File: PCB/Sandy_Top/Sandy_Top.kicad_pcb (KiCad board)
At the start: 2 copper layers, 285 x 37 mm, 63 parts, among them J1 Conn_02x02_Top_Bottom, J2 Conn_02x02_Top_Bottom, J3 Conn_02x02_Top_Bottom

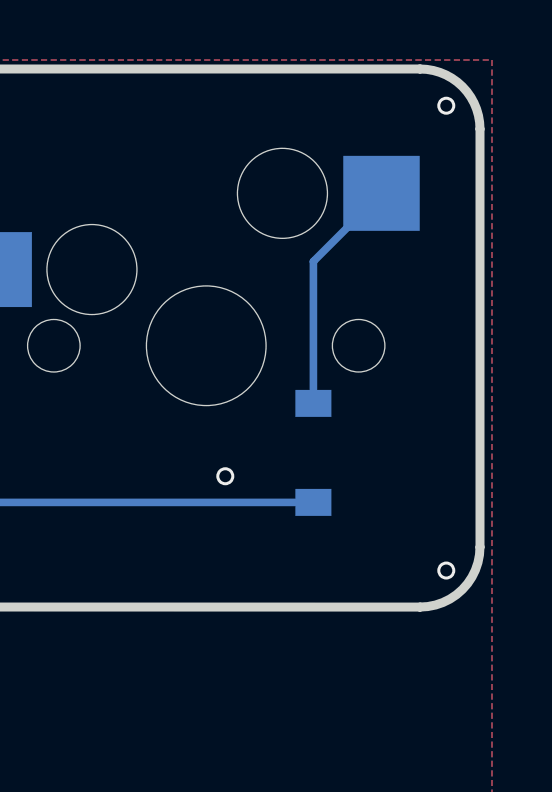
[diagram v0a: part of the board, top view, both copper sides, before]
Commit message: Topの3キーの並び順が間違えているが、互換性を保つため、修正しないコメントを追加
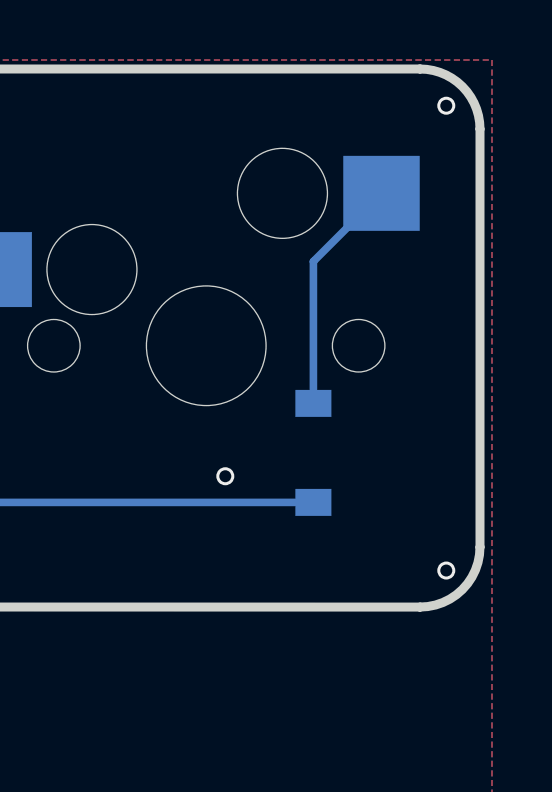
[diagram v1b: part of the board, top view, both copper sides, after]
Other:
- board text added: "SW_6, `, \ の3個の並び順が間違っているが、 v01とのソフト的な互換性を保つため、修正はおこなわない。"
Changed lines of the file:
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@@
     (fp_arc (start 37.375 16.24996) (mid 36.789208 17.664168) (end 35.375 18.24996)
       (stroke (width 0.3) (type solid)) (layer "Edge.Cuts"))
-    (fp_arc (start 140.475 -18.75004) (mid 141.889222 -18.164279) (end 142.475 -16.75004)
+    (fp_arc (start 140.475 -18.75004) (mid 141.889257 -18.164285) (end 142.475 -16.75004)
       (stroke (width 0.3) (type solid)) (layer "Edge.Cuts"))
-    (fp_arc (start 142.475 -2.814254) (mid 141.889197 -1.40007) (end 140.475 -0.814254)
+    (fp_arc (start 142.475 -2.814254) (mid 141.889203 -1.400035) (end 140.475 -0.814254)
       (stroke (width 0.3) (type solid)) (layer "Edge.Cuts"))
     (fp_circle (center -47.625 -14.50004) (end -45.425 -14.50004)
@@
     (effects (font (size 1 1) (thickness 0.15)))
   )
+  (gr_text "SW_6, `, \\　の3個の並び順が間違っているが、\nv01とのソフト的な互換性を保つため、修正はおこなわない。" (at 134.540625 14.2875) (layer "Eco2.User")
+    (effects (font (size 1.5 1.5) (thickness 0.1875)) (justify left bottom))
+  )
   (gr_text "to Mid" (at 177.03031 52.00653) (layer "Eco2.User")

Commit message: WIP ネジ穴位置、スイッチ位置調整中
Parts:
- removed D15: D, locallib:D_SOD-123_Emphasized_Direction_Line
- removed EXT_TC7: Conn_01x01, TestPoint:TestPoint_THTPad_D2.0mm_Drill1.0mm
- removed the SW_=1 at (291.3, 27.0)
- added H10: MountingHole, locallib:MountingHole_2.2mm_M2_Pad_minimal, F.Cu at (138.1, -8.33)
- added H9: MountingHole, locallib:MountingHole_2.2mm_M2_Pad_minimal, F.Cu at (132.1, -8.33)
- moved SW_INS1 9.53 mm to (281.8, 27.0)
- moved D10 9.53 mm to (209.2, 31.6)
- moved D11 9.53 mm to (228.2, 30.6)
- moved D12 9.53 mm to (247.3, 31.6)
- moved D2 9.53 mm to (56.8, 31.6)
- moved D3 9.53 mm to (75.8, 30.6)
- moved D7 9.53 mm to (190.1, 30.6)
- moved D8 9.53 mm to (152.0, 30.5)
- moved SW_-1 9.53 mm to (148.5, 27.0)
- moved SW_10 9.53 mm to (262.8, 27.0)
- moved SW_3 9.53 mm to (91.3, 27.0)
- moved SW_4 9.53 mm to (110.4, 27.0)
- moved SW_6 9.53 mm to (186.6, 27.0)
- moved SW_7 9.53 mm to (205.6, 27.0)
- moved SW_9 9.53 mm to (243.7, 27.0)
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- renumbered SW_`1 to SW_-1, SW_\1 to SW_=1, SW_-1 to SW_INS1
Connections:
- J1 pad 4: Top_col7 -> unconnected-(J1-Pin_4-Pad4)_1
- SW_-1 pad 2: Net-(D8-A) -> Net-(D7-A)
- SW_6 pad 1: Top_col3 -> Top_col4
- SW_6 pad 2: Net-(D7-A) -> Net-(D9-A)
- SW_=1 pad 1: Top_col4 -> Top_col3
- SW_=1 pad 2: Net-(D9-A) -> Net-(D8-A)
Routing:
- net Top_row0: track 276.6 -> 0.00 mm
- net Top_row5: track 244.0 -> 0.00 mm
- net Top_col7: track 136.6 -> 0.00 mm, vias 2 -> 0
- net Top_col0: track 125.7 -> 0.00 mm, vias 1 -> 0
- net Top_col6: track 109.5 -> 0.00 mm
- net Top_col3: track 99.5 -> 0.00 mm, vias 1 -> 0
- net Top_col1: track 91.3 -> 0.00 mm, vias 1 -> 0
- net Top_col2: track 75.5 -> 0.00 mm, vias 1 -> 0
- net Top_col5: track 72.9 -> 0.00 mm, vias 1 -> 0
- net Top_col4: track 68.0 -> 0.00 mm, vias 2 -> 0
- net Top_row6: track 57.1 -> 0.00 mm, vias 1 -> 0
- net Top_row1: track 47.0 -> 0.00 mm, vias 1 -> 0
- net Net-(D19-A): track 19.4 -> 0.00 mm
- net Net-(D12-A): track 9.00 -> 0.00 mm
- net Net-(D10-A): track 9.00 -> 0.00 mm
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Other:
- board text added: "左右端のスイッチの外側にネジ穴を追加。"
- board text removed: "SW_6, `, \ の3個の並び順が間違っているが、 v01とのソフト的な互換性を保つため、修正はおこなわない。"

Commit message: Topネジ穴を仮配置
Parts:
- added H11: MountingHole, locallib:MountingHole_2.2mm_M2_Pad_minimal, B.Cu at (138.9, 52.0)
- added H12: MountingHole, locallib:MountingHole_2.2mm_M2_Pad_minimal, B.Cu at (177.0, 52.0)
- H10, H9: moved to B.Cu
- SW_4, SW_INS1: footprint MX_Alps_Hybrid:MXOnly-1U-Hotswap-guide -> MX_Alps_Hybrid:MXOnly-1U-Hotswap-screw-hole-side1-guide
- SW_5: footprint MX_Alps_Hybrid:MXOnly-1U-Hotswap-screw-hole-side2-guide -> MX_Alps_Hybrid:MXOnly-1U-Hotswap-guide
- SW_8: footprint MX_Alps_Hybrid:MXOnly-1U-Hotswap-screw-hole-side3-guide -> MX_Alps_Hybrid:MXOnly-1U-Hotswap-guide
- moved H6 219.1 mm to (62.7, 28.2)
- moved H4 200.2 mm to (291.3, 20.6), turned to 0 degrees
- moved H5 200.1 mm to (24.6, 33.0)
- moved H3 162.1 mm to (196.1, 20.6), turned to 0 degrees
- moved H10 158.7 mm to (291.3, 33.0), turned to 180 degrees
- moved H9 126.5 mm to (253.2, 28.2), turned to 180 degrees
- moved H1 104.8 mm to (24.6, 20.6)
- moved H2 66.7 mm to (119.9, 20.6)
- moved H8 44.9 mm to (215.1, 28.2)
- moved H7 44.9 mm to (100.8, 28.2)
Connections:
- H1 pad 1: Top_GND -> unconnected-(H1-Pad1)
- H10 pad 1: Top_GND -> unconnected-(H10-Pad1)
- H2 pad 1: Top_GND -> unconnected-(H2-Pad1)
- H3 pad 1: Top_GND -> unconnected-(H3-Pad1)
- H4 pad 1: Top_GND -> unconnected-(H4-Pad1)
- H5 pad 1: Top_GND -> unconnected-(H5-Pad1)
- H6 pad 1: Top_GND -> unconnected-(H6-Pad1)
- H7 pad 1: Top_GND -> unconnected-(H7-Pad1)
- H8 pad 1: Top_GND -> unconnected-(H8-Pad1)
- H9 pad 1: Top_GND -> unconnected-(H9-Pad1)
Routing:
- added copper zone on B.Cu, net unconnected-(H9-Pad1)
- added copper zone on F.Cu, net unconnected-(H9-Pad1)
- removed copper zone on B.Cu, net Top_GND
- removed copper zone on F.Cu, net Top_GND
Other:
- board text removed: "左右端のスイッチの外側にネジ穴を追加。"

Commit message: ネジ穴調整、追加
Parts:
- added Cutout1: 60_Outline, locallib:60_Outline-Sandy-Mid7-narrow-bottom-small-right-hole, F.Cu at (155.6, -33.7)
- added D1: D, locallib:D_SOD-123_Emphasized_Direction_Line, B.Cu at (29.4, -51.6)
- added D10: D, locallib:D_SOD-123_Emphasized_Direction_Line, B.Cu at (186.6, -32.5)
- added D11: D, locallib:D_SOD-123_Emphasized_Direction_Line, B.Cu at (138.9, -13.5)
- added D12: D, locallib:D_SOD-123_Emphasized_Direction_Line, B.Cu at (158.0, -13.5)
- added D13: D, locallib:D_SOD-123_Emphasized_Direction_Line, B.Cu at (173.5, -13.5)
- added D2: D, locallib:D_SOD-123_Emphasized_Direction_Line, B.Cu at (53.2, -51.6)
- added D3: D, locallib:D_SOD-123_Emphasized_Direction_Line, B.Cu at (110.4, -51.6)
- added D4: D, locallib:D_SOD-123_Emphasized_Direction_Line, B.Cu at (205.1, -51.6)
- added D5: D, locallib:D_SOD-123_Emphasized_Direction_Line, B.Cu at (262.8, -51.6)
- added D6: D, locallib:D_SOD-123_Emphasized_Direction_Line, B.Cu at (279.4, -50.4)
- added D7: D, locallib:D_SOD-123_Emphasized_Direction_Line, B.Cu at (123.5, -32.5)
- added D8: D, locallib:D_SOD-123_Emphasized_Direction_Line, B.Cu at (131.1, -32.5)
- added D9: D, locallib:D_SOD-123_Emphasized_Direction_Line, B.Cu at (179.4, -32.5)
- added EXT_MC0: Conn_01x01, TestPoint:TestPoint_THTPad_D2.0mm_Drill1.0mm, B.Cu at (93.7, -68.2)
- added EXT_MC2: Conn_01x01, TestPoint:TestPoint_THTPad_D2.0mm_Drill1.0mm, B.Cu at (97.3, -68.2)
- added EXT_MC3: Conn_01x01, TestPoint:TestPoint_THTPad_D2.0mm_Drill1.0mm, B.Cu at (100.8, -68.2)
- added EXT_MC4: Conn_01x01, TestPoint:TestPoint_THTPad_D2.0mm_Drill1.0mm, B.Cu at (210.4, -68.2)
- added EXT_MC6: Conn_01x01, TestPoint:TestPoint_THTPad_D2.0mm_Drill1.0mm, B.Cu at (213.9, -68.2)
- added EXT_MR1: Conn_01x01, TestPoint:TestPoint_THTPad_D2.0mm_Drill1.0mm, B.Cu at (41.3, -55.1)
- added EXT_MR2: Conn_01x01, TestPoint:TestPoint_THTPad_D2.0mm_Drill1.0mm, B.Cu at (196.1, -68.2)
- added EXT_MR3: Conn_01x01, TestPoint:TestPoint_THTPad_D2.0mm_Drill1.0mm, B.Cu at (178.2, -68.2)
- added EXT_MR6: Conn_01x01, TestPoint:TestPoint_THTPad_D2.0mm_Drill1.0mm, B.Cu at (47.3, -55.1)
- added EXT_MR7: Conn_01x01, TestPoint:TestPoint_THTPad_D2.0mm_Drill1.0mm, B.Cu at (192.5, -68.2)
- added EXT_MR8: Conn_01x01, TestPoint:TestPoint_THTPad_D2.0mm_Drill1.0mm, B.Cu at (174.6, -68.2)
- added H1: MountingHole, locallib:MountingHole_2.2mm_M2_Pad_minimal, F.Cu at (16.3, -68.7)
- added H10: MountingHole, locallib:MountingHole_2.2mm_M2_Pad_minimal, F.Cu at (254.4, -53.8)
- added H11: MountingHole, locallib:MountingHole_2.2mm_M2_Pad_minimal, F.Cu at (16.3, -37.3)
- added H12: MountingHole, locallib:MountingHole_2.2mm_M2_Pad_minimal, F.Cu at (294.9, -37.3)
- added H13: MountingHole, locallib:MountingHole_2.2mm_M2_Pad_minimal, F.Cu at (117.5, -37.3)
- added H14: MountingHole, locallib:MountingHole_2.2mm_M2_Pad_minimal, F.Cu at (193.7, -37.2)
- added H15: MountingHole, locallib:MountingHole_2.2mm_M2_Pad_minimal, F.Cu at (130.6, -14.7)
- added H16: MountingHole, locallib:MountingHole_2.2mm_M2_Pad_minimal, F.Cu at (180.6, -14.7)
- added H2: MountingHole, locallib:MountingHole_2.2mm_M2_Pad_minimal, F.Cu at (69.9, -68.7)
- added H3: MountingHole, locallib:MountingHole_2.2mm_M2_Pad_minimal, F.Cu at (127.0, -68.7)
- added H4: MountingHole, locallib:MountingHole_2.2mm_M2_Pad_minimal, F.Cu at (184.2, -68.7)
- added H5: MountingHole, locallib:MountingHole_2.2mm_M2_Pad_minimal, F.Cu at (241.3, -68.7)
- added H6: MountingHole, locallib:MountingHole_2.2mm_M2_Pad_minimal, F.Cu at (294.9, -68.7)
- added H7: MountingHole, locallib:MountingHole_2.2mm_M2_Pad_minimal, F.Cu at (88.9, -56.3)
- added H8: MountingHole, locallib:MountingHole_2.2mm_M2_Pad_minimal, F.Cu at (222.3, -56.3)
- added H9: MountingHole, locallib:MountingHole_2.2mm_M2_Pad_minimal, F.Cu at (56.8, -53.8)
- added H_top_1: MountingHole, locallib:MountingHole_2.2mm_M2_Pad_minimal, B.Cu at (22.2, -68.7)
- added H_top_10: MountingHole, locallib:MountingHole_2.2mm_M2_Pad_minimal, B.Cu at (288.9, -56.3)
- added H_top_11: MountingHole, locallib:MountingHole_2.2mm_M2_Pad_minimal, B.Cu at (136.5, -37.3)
- added H_top_12: MountingHole, locallib:MountingHole_2.2mm_M2_Pad_minimal, B.Cu at (174.6, -37.3)
- added H_top_2: MountingHole, locallib:MountingHole_2.2mm_M2_Pad_minimal, B.Cu at (117.5, -68.7)
- added H_top_3: MountingHole, locallib:MountingHole_2.2mm_M2_Pad_minimal, B.Cu at (193.7, -68.7)
- added H_top_4: MountingHole, locallib:MountingHole_2.2mm_M2_Pad_minimal, B.Cu at (288.9, -68.7)
- added H_top_5: MountingHole, locallib:MountingHole_2.2mm_M2_Pad_minimal, B.Cu at (22.2, -56.3)
- added H_top_6: MountingHole, locallib:MountingHole_2.2mm_M2_Pad_minimal, B.Cu at (60.3, -61.1)
- added H_top_7: MountingHole, locallib:MountingHole_2.2mm_M2_Pad_minimal, B.Cu at (98.4, -61.1)
- added H_top_8: MountingHole, locallib:MountingHole_2.2mm_M2_Pad_minimal, B.Cu at (212.7, -61.1)
- added H_top_9: MountingHole, locallib:MountingHole_2.2mm_M2_Pad_minimal, B.Cu at (250.8, -61.1)
- added J1: Conn_02x02_Top_Bottom, locallib:JST_SH_SM04B-SRSS-TB_1x04-1MP_P1.00mm_Horizontal_wCable_housing_spare_pin, B.Cu at (190.5, -56.3)
- added J2: Conn_02x02_Top_Bottom, locallib:JST_SH_SM04B-SRSS-TB_1x04-1MP_P1.00mm_Horizontal_wCable_housing_spare_pin, B.Cu at (190.5, -45.6)
- added J3: Conn_02x02_Top_Bottom, locallib:JST_SH_SM04B-SRSS-TB_1x04-1MP_P1.00mm_Horizontal_wCable_housing_spare_pin, B.Cu at (119.9, -45.6)
- added REF**: 60_Outline, locallib:60_Outline-Sandy-Top-NoSwImage-WithHole2-ECO1, F.Cu at (155.6, -52.8)
- added SW_'1: SW_Push, MX_Alps_Hybrid:MXOnly-1U-Hotswap-guide, F.Cu at (165.1, -24.2)
- added SW_;1: SW_Push, MX_Alps_Hybrid:MXOnly-1U-Hotswap-guide, F.Cu at (146.1, -24.2)
- added SW_BS1: SW_Push, MX_Alps_Hybrid:MXOnly-1U-Hotswap-guide, F.Cu at (279.4, -43.2)
- added SW_G1: SW_Push, MX_Alps_Hybrid:MXOnly-1U-Hotswap-guide, F.Cu at (127.0, -24.2)
- added SW_H1: SW_Push, MX_Alps_Hybrid:MXOnly-1U-Hotswap-guide, F.Cu at (184.2, -24.2)
- added SW_P1: SW_Push, MX_Alps_Hybrid:MXOnly-1U-Hotswap-guide, F.Cu at (260.4, -43.2)
- added SW_Q1: SW_Push, MX_Alps_Hybrid:MXOnly-1U-Hotswap-guide, F.Cu at (50.8, -43.2)
- added SW_R1: SW_Push, MX_Alps_Hybrid:MXOnly-1U-Hotswap-guide, F.Cu at (108.0, -43.2)
- added SW_R4CNT_C1: SW_Push, MX_Alps_Hybrid:MXOnly-1U-Hotswap-guide, F.Cu at (155.6, -5.14)
- added SW_R4CNT_L1: SW_Push, MX_Alps_Hybrid:MXOnly-1U-Hotswap-guide, F.Cu at (136.5, -5.14)
- added SW_R4CNT_R1: SW_Push, MX_Alps_Hybrid:MXOnly-1U-Hotswap-guide, F.Cu at (174.6, -5.14)
- added SW_TAB1: SW_Push, MX_Alps_Hybrid:MXOnly-1U-Hotswap-guide, F.Cu at (31.8, -43.2)
- added SW_U1: SW_Push, MX_Alps_Hybrid:MXOnly-1U-Hotswap-guide, F.Cu at (203.2, -43.2)
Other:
- board size 285 x 37 mm -> 285 x 73.4 mm
- board text added: "#Sandy_kbd DN0030, Mid by @jpskenn"
- board text added: "Mid 1"
- board text added: "Mid 2"
- board text added: "Mid 3"
- board text added: "Screw to Bottom ↓"
- board text added: "to Top"
